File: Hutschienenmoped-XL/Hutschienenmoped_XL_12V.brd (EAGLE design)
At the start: 96.3 x 101.8 mm, 126 parts, among them J1 638207222005, J13 638207222005, J15 638207222008, J2 645004114822, J4 61300421121, J7 638207222005, J8 638207222007, U4 TLE9250VSJ

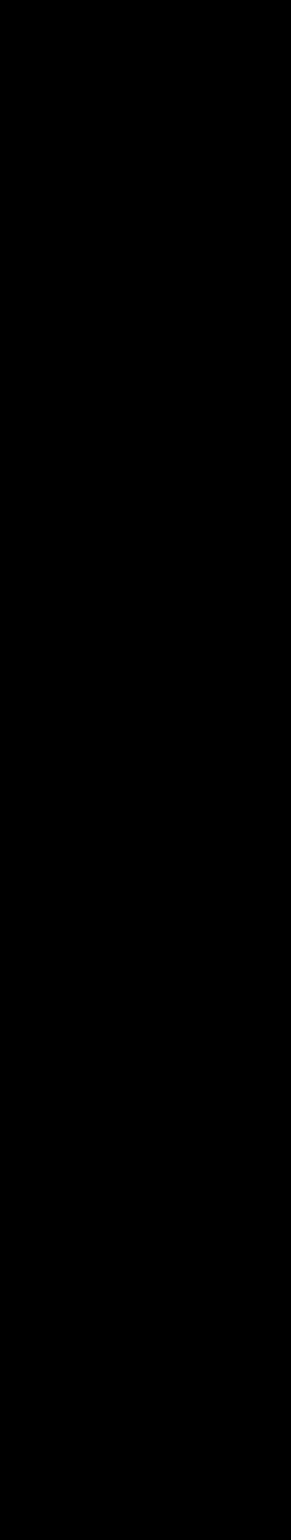
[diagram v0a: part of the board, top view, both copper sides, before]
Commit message: gitflow-feature-stash: prot Add SMA_DO-214AC package, elements D014 to D023 with attributes, and resistors R35 to R38. Update classes Ampere7 and clearance values. Include wire connections for new elements in signals Q3, Q1C, Q1, AGNDU3, and 5V.
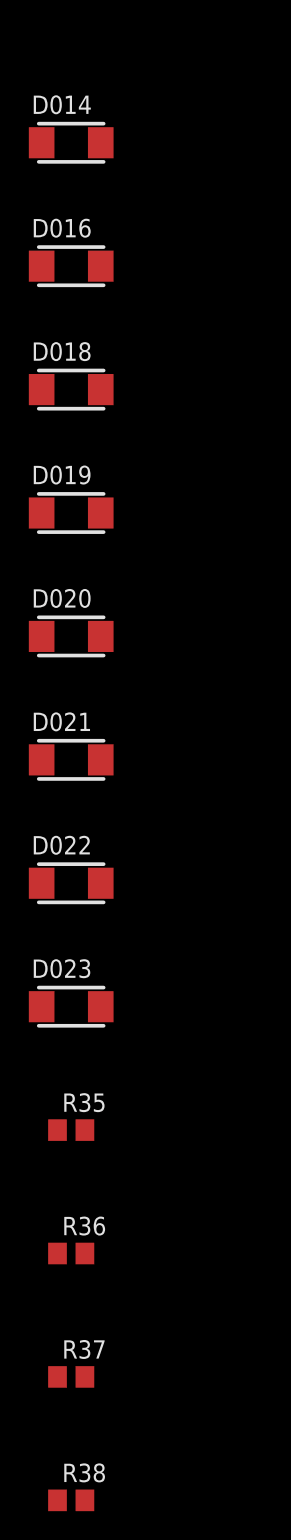
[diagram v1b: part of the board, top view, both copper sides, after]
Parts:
- added D014, D016, D018, D019, D020, D021, D022, D023: GS1J-L, fliegl-elektronik:SMA_DO-214AC
- added R35, R36, R37, R38: 1k2, resistor:R0805
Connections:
- new net N$16: R38.2, U6.4
- new net N$20: R35.2, U2.4
- new net N$21: R36.2, U3.4
- new net N$7: R37.2, U5.4
- net ECU_GND: now also R35.1, R36.1, R37.1, R38.1
- net PWR_GND: now also D014.A, D016.A, D018.A, D019.A, D020.A, D021.A, D022.A, D023.A
- net Q1: now also D014.C
- net Q2: now also D019.C
- net Q3: now also D016.C
- net Q4: now also D018.C
- net Q5: now also D020.C
- net Q6: now also D021.C
- net Q7: now also D022.C
- net Q8: now also D023.C

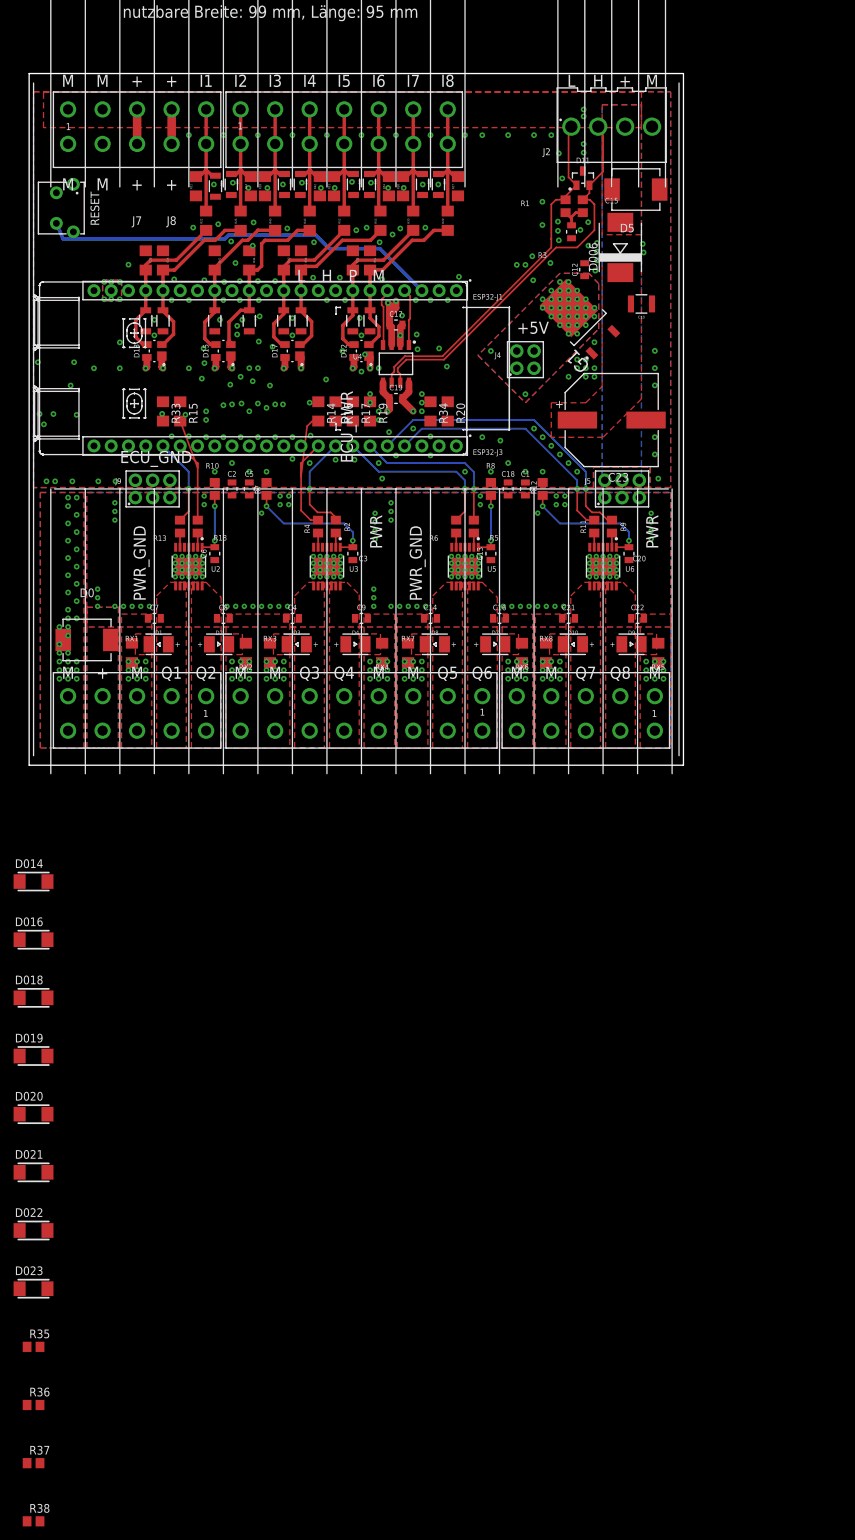
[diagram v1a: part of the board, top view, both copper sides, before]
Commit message: Update editor types and views, wire bend settings, polygon ranks, layers, grid distances, and element attributes. Adjusted grid distance unit and layer numbers for elements C8 and C4.
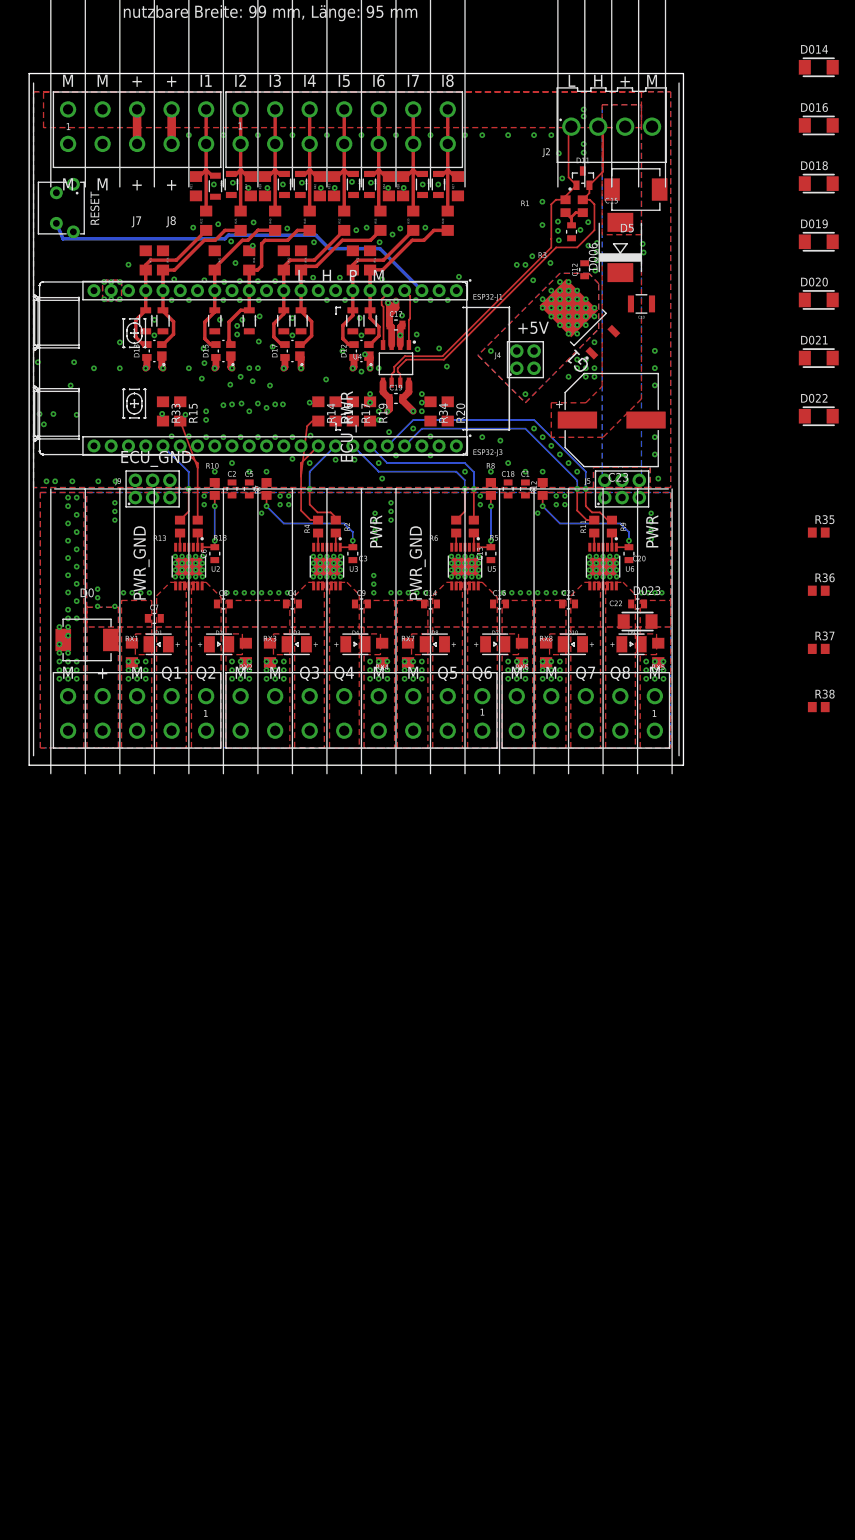
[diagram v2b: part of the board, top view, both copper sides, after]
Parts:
- moved D014 166.5 mm to (115.6, 102.7)
- moved D016 166.5 mm to (115.6, 94.2)
- moved D018 166.5 mm to (115.6, 85.6)
- moved D019 166.5 mm to (115.6, 77.0)
- moved D020 166.5 mm to (115.6, 68.5)
- moved D021 166.5 mm to (115.6, 59.9)
- moved D022 166.5 mm to (115.6, 51.4)
- moved R35 166.5 mm to (115.6, 34.2)
- moved R36 166.5 mm to (115.6, 25.7)
- moved R37 166.5 mm to (115.6, 17.1)
- moved R38 166.5 mm to (115.6, 8.56)
- moved D023 132.5 mm to (88.9, 21.1)
- moved C14 2.13 mm to (58.4, 23.7)
- moved C16 2.13 mm to (68.6, 23.7)
- moved C21 2.13 mm to (78.7, 23.7)
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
